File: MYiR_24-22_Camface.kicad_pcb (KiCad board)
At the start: 2 copper layers, 30 x 30 mm, 12 parts, among them J1 Conn_01x22_FPC_0.5mm, J2 Conn_01x24_FPC

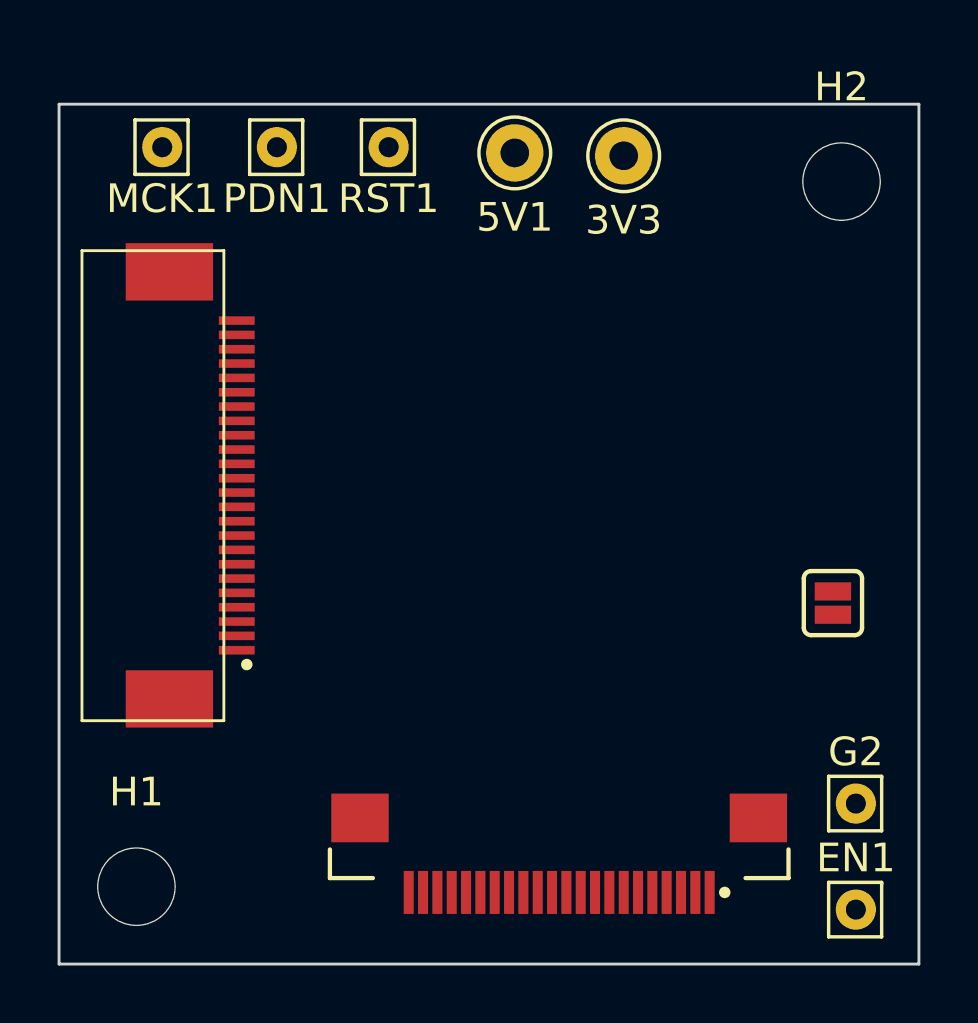
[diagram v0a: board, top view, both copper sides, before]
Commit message: Route all PCB signals
Co-Authored-By: Claude Sonnet 5.5 <noreply@anthropic.com>
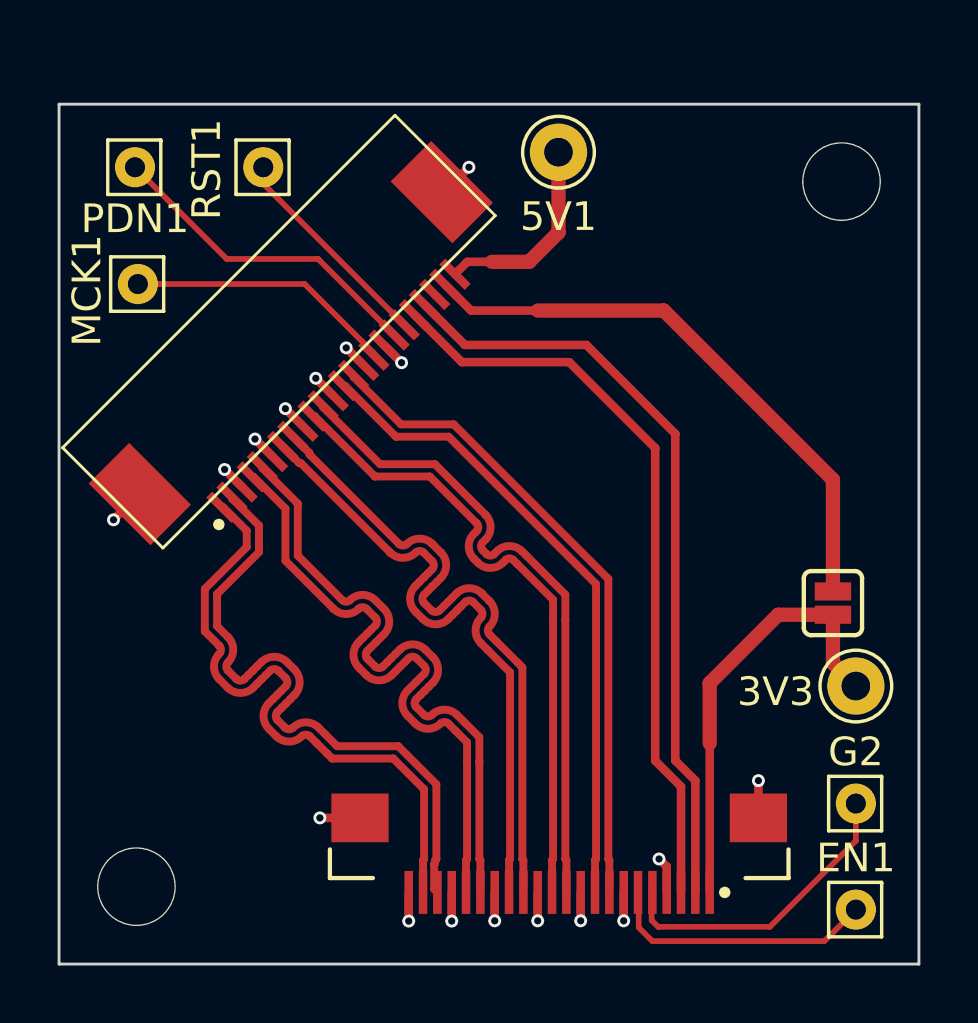
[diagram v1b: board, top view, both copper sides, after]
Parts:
- moved 3V3 20.2 mm to (132.8, 95.3)
- moved J2 6.56 mm to (113.0, 83.3), turned to -135 degrees
- moved PDN1 5.00 mm to (107.7, 77.2)
- moved MCK1 4.85 mm to (107.8, 81.3)
- moved RST1 4.43 mm to (112.1, 77.2)
- moved 5V1 1.53 mm to (122.4, 76.7)
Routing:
- net /SDA: track 0.00 -> 26.9 mm
- net /SCL: track 0.00 -> 26.2 mm
- net /D3P: track 0.00 -> 22.8 mm
- net /D2P: track 0.00 -> 22.7 mm
- net /D0P: track 0.00 -> 22.7 mm
- net /CKP: track 0.00 -> 22.7 mm
- net /D1P: track 0.00 -> 22.6 mm
- net /D3N: track 0.00 -> 22.5 mm
- net /D2N: track 0.00 -> 22.4 mm
- net /CKN: track 0.00 -> 22.3 mm
- net /D0N: track 0.00 -> 22.3 mm
- net /D1N: track 0.00 -> 22.3 mm
- net Net-(J2-Pin_23): track 0.00 -> 20.3 mm
- net GND: track 0.00 -> 17.7 mm, vias 0 -> 17
- net +3.3V: track 0.00 -> 15.4 mm
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- added copper zone on B.Cu, net GND
